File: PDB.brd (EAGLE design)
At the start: 125.9 x 103 mm, 76 parts

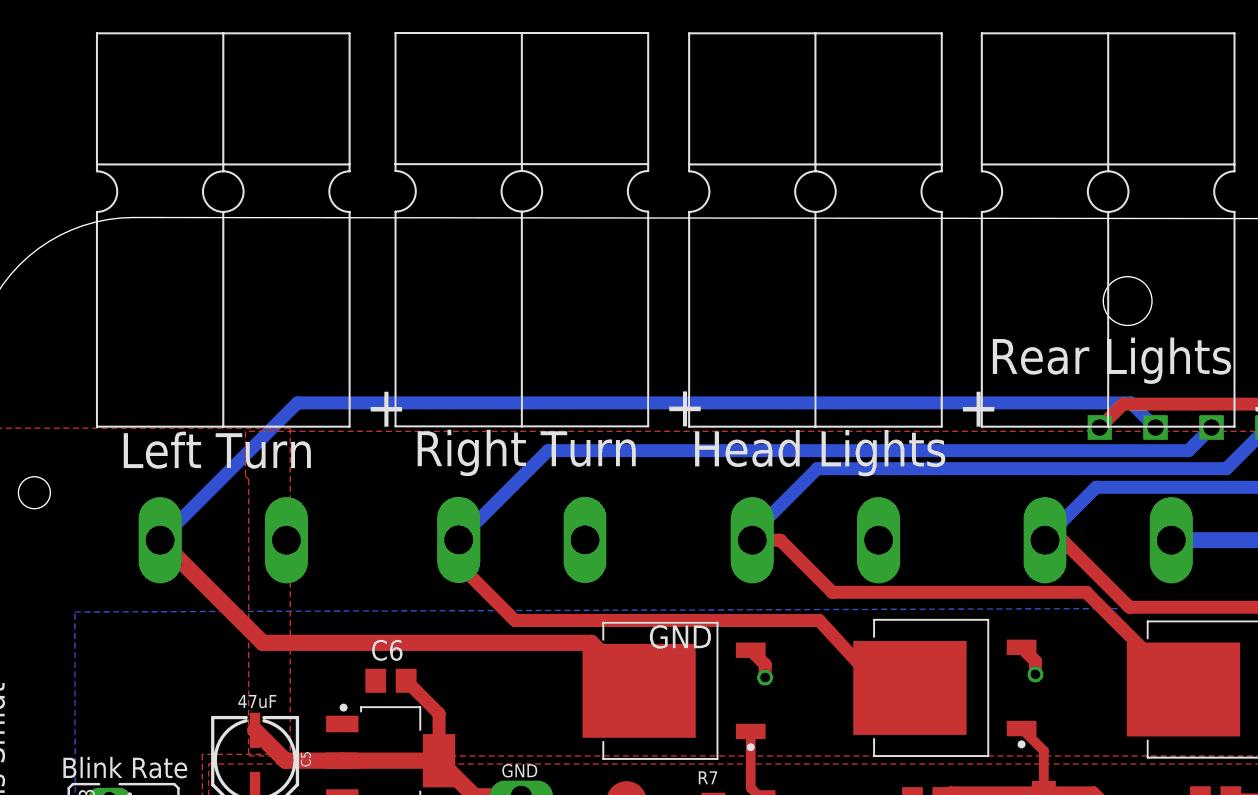
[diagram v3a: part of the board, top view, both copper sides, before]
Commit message: Deleted Anderson connector for left and right light
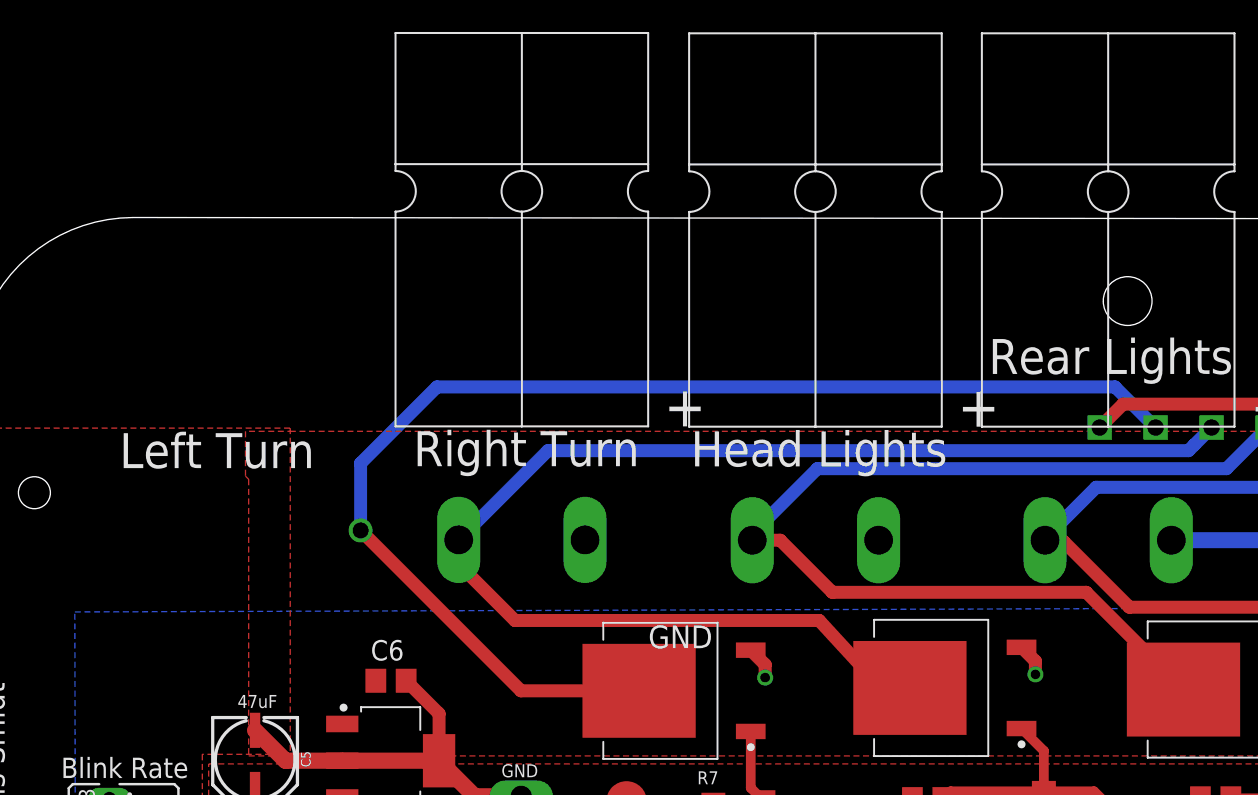
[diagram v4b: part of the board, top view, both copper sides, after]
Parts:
- removed HAZL_OUT: POWERPOLE_POWER25A_HORIZONTAL_G2, powerpoles:POWERPOLE_PAIR_25A_HORIZ_G2
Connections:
- net HAZ_L_SIG: no longer HAZL_OUT.BLACK
- net VDD: no longer HAZL_OUT.RED
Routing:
- net HAZ_L_SIG: track 100.3 -> 78.5 mm, vias 0 -> 1
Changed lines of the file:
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@@
 <drawing>
 <settings>
-<setting alwaysvectorfont="no"/>
+<setting alwaysvectorfont="yes"/>
 <setting verticaltext="up"/>
 </settings>
@@
 <text x="91.5" y="134.82" size="0.6096" layer="26">GND</text>
 <text x="80.06" y="131.94" size="0.6096" layer="26">TURN_R</text>
-<text x="76.94" y="134.76" size="0.6096" layer="26">TURN_L</text>
+<text x="77.04" y="134.56" size="0.6096" layer="26">TURN_L</text>
 <text x="73.52" y="134.76" size="0.6096" layer="26">BRAKE</text>
 <text x="84.9" y="131.94" size="0.6096" layer="26">HL</text>
@@
 <element name="ADD1_OUT" library="powerpoles" package="POWERPOLE_PAIR_25A_HORIZ_G2" value="POWERPOLE_POWER25A_HORIZONTAL_G2" x="55.604" y="52.08" smashed="yes" rot="R180"/>
 <element name="WIPER_OUT" library="powerpoles" package="POWERPOLE_PAIR_25A_HORIZ_G2" value="POWERPOLE_POWER25A_HORIZONTAL_G2" x="35.64" y="51.84" smashed="yes" rot="R180"/>
-<element name="HAZL_OUT" library="powerpoles" package="POWERPOLE_PAIR_25A_HORIZ_G2" value="POWERPOLE_POWER25A_HORIZONTAL_G2" x="20.012" y="133.69" smashed="yes"/>
 <element name="HAZR_OUT" library="powerpoles" package="POWERPOLE_PAIR_25A_HORIZ_G2" value="POWERPOLE_POWER25A_HORIZONTAL_G2" x="38.684" y="133.71" smashed="yes"/>
 <element name="BRAKE_OUT" library="powerpoles" package="POWERPOLE_PAIR_25A_HORIZ_G2" value="POWERPOLE_POWER25A_HORIZONTAL_G2" x="96.232" y="133.49" smashed="yes"/>
@@
 <signals>
 <signal name="VDD">
-<contactref element="HAZL_OUT" pad="RED"/>
 <contactref element="HAZR_OUT" pad="RED"/>
 <contactref element="HEADLIGHTS_OUT" pad="RED"/>
@@
 </signal>
 <signal name="HAZ_L_SIG">
-<contactref element="HAZ_L" pad="3"/>
-<contactref element="HAZL_OUT" pad="BLACK"/>
 <contactref element="LIGHTS" pad="P2"/>
-<wire x1="76.776" y1="135.176" x2="24.648" y2="135.176" width="0.8128" layer="16"/>
-<wire x1="24.648" y1="135.176" x2="16.062" y2="126.59" width="0.8128" layer="16"/>
-<wire x1="78.316" y1="133.636" x2="76.776" y2="135.176" width="0.8128" layer="16"/>
-<wire x1="43.01668125" y1="120.172" x2="22.48" y2="120.172" width="1.016" layer="1"/>
-<wire x1="22.48" y1="120.172" x2="16.062" y2="126.59" width="1.016" layer="1"/>
-<wire x1="46.01668125" y1="117.172" x2="43.01668125" y2="120.172" width="1.016" layer="1"/>
+<wire x1="75.776" y1="136.176" x2="78.316" y2="133.636" width="0.8128" layer="16"/>
+<contactref element="HAZ_L" pad="3"/>
+<wire x1="46.01668125" y1="117.172" x2="38.628" y2="117.172" width="0.8128" layer="1"/>
+<via x="28.6" y="127.2" extent="1-16" drill="1"/>
+<wire x1="38.628" y1="117.172" x2="28.6" y2="127.2" width="0.8128" layer="1"/>
+<wire x1="28.6" y1="127.2" x2="28.6" y2="131.4" width="0.8128" layer="16"/>
+<wire x1="33.376" y1="136.176" x2="75.776" y2="136.176" width="0.8128" layer="16"/>
+<wire x1="28.6" y1="131.4" x2="33.376" y2="136.176" width="0.8128" layer="16"/>
 </signal>
 <signal name="BRAKE_SIG">

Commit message: Last time forget to save. This is the real version of last commit.
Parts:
- removed ADD1_OUT, HAZR_OUT: POWERPOLE_POWER25A_HORIZONTAL_G2, powerpoles:POWERPOLE_PAIR_25A_HORIZ_G2
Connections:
- removed net N$17: ADD1.3, ADD1_OUT.BLACK
- net HAZ_R_SIG: no longer HAZR_OUT.BLACK
- net VDD: no longer ADD1_OUT.RED, HAZR_OUT.RED
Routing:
- net HAZ_L_SIG: track 78.5 -> 50.2 mm
- net HAZ_R_SIG: track 83.0 -> 58.4 mm, vias 0 -> 1
- net N$17: track 8.79 -> 0.00 mm
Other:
- board text removed: "Left Turn"
- board text removed: "Right Turn"
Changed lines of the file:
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@@
 <text x="7.287" y="86.841" size="2.54" layer="25" font="vector" ratio="13" rot="R90">SEM 2019</text>
 <text x="8.21" y="56.622" size="3.81" layer="25" rot="R90">REVolution</text>
-<text x="31.904" y="131.22" size="2.1844" layer="25">Right Turn </text>
-<text x="13.52" y="131.1" size="2.1844" layer="25">Left Turn </text>
 <text x="64.746" y="64.275" size="1.27" layer="25">GND</text>
 <text x="46.588" y="119.834" size="1.4224" layer="25">GND</text>
@@
 <elements>
 <element name="ADD1" library="master_library" package="TO254P1054X240-3" package3d_urn="urn:adsk.eagle:package:8893803/1" value="NCV8405ADPAK-3PIN" x="56.654" y="68.958" smashed="yes" rot="R270"/>
-<element name="ADD1_OUT" library="powerpoles" package="POWERPOLE_PAIR_25A_HORIZ_G2" value="POWERPOLE_POWER25A_HORIZONTAL_G2" x="55.604" y="52.08" smashed="yes" rot="R180"/>
 <element name="WIPER_OUT" library="powerpoles" package="POWERPOLE_PAIR_25A_HORIZ_G2" value="POWERPOLE_POWER25A_HORIZONTAL_G2" x="35.64" y="51.84" smashed="yes" rot="R180"/>
-<element name="HAZR_OUT" library="powerpoles" package="POWERPOLE_PAIR_25A_HORIZ_G2" value="POWERPOLE_POWER25A_HORIZONTAL_G2" x="38.684" y="133.71" smashed="yes"/>
 <element name="BRAKE_OUT" library="powerpoles" package="POWERPOLE_PAIR_25A_HORIZ_G2" value="POWERPOLE_POWER25A_HORIZONTAL_G2" x="96.232" y="133.49" smashed="yes"/>
 <element name="HEADLIGHTS_OUT" library="powerpoles" package="POWERPOLE_PAIR_25A_HORIZ_G2" value="POWERPOLE_POWER25A_HORIZONTAL_G2" x="57.044" y="133.69" smashed="yes"/>
@@
 <signals>
 <signal name="VDD">
-<contactref element="HAZR_OUT" pad="RED"/>
 <contactref element="HEADLIGHTS_OUT" pad="RED"/>
 <contactref element="C10" pad="+"/>
 <contactref element="D1" pad="C"/>
-<contactref element="ADD1_OUT" pad="RED"/>
 <contactref element="LM2940" pad="1"/>
 <contactref element="TRACO" pad="1"/>
@@
 <wire x1="106" y1="126.952" x2="99.316" y2="133.636" width="1.27" layer="16"/>
 </signal>
-<signal name="N$17">
-<contactref element="ADD1" pad="3"/>
-<contactref element="ADD1_OUT" pad="BLACK"/>
-<wire x1="59.554" y1="59.18" x2="56.654" y2="62.08" width="1.27" layer="1"/>
-<wire x1="56.654" y1="62.08" x2="56.654" y2="66.773" width="1.27" layer="1"/>
-</signal>
 <signal name="N$19">
 <contactref element="WIPER_" pad="3"/>
@@
 <signal name="HAZ_L_SIG">
 <contactref element="LIGHTS" pad="P2"/>
-<wire x1="75.776" y1="136.176" x2="78.316" y2="133.636" width="0.8128" layer="16"/>
 <contactref element="HAZ_L" pad="3"/>
-<wire x1="46.01668125" y1="117.172" x2="38.628" y2="117.172" width="0.8128" layer="1"/>
-<via x="28.6" y="127.2" extent="1-16" drill="1"/>
-<wire x1="38.628" y1="117.172" x2="28.6" y2="127.2" width="0.8128" layer="1"/>
-<wire x1="28.6" y1="127.2" x2="28.6" y2="131.4" width="0.8128" layer="16"/>
-<wire x1="33.376" y1="136.176" x2="75.776" y2="136.176" width="0.8128" layer="16"/>
-<wire x1="28.6" y1="131.4" x2="33.376" y2="136.176" width="0.8128" layer="16"/>
+<via x="46.1" y="127.2" extent="1-16" drill="0.8128"/>
+<wire x1="46.1" y1="127.2" x2="46.1" y2="117.25531875" width="0.8128" layer="1"/>
+<wire x1="46.01668125" y1="117.172" x2="46.1" y2="117.25531875" width="0.8128" layer="1"/>
+<wire x1="46.1" y1="127.2" x2="46.1" y2="132.5" width="0.8128" layer="16"/>
+<wire x1="46.1" y1="132.5" x2="49.8" y2="136.2" width="0.8128" layer="16"/>
+<wire x1="49.8" y1="136.2" x2="75.752" y2="136.2" width="0.8128" layer="16"/>
+<wire x1="75.752" y1="136.2" x2="78.316" y2="133.636" width="0.8128" layer="16"/>
 </signal>
 <signal name="BRAKE_SIG">
@@
 <contactref element="LIGHTS" pad="P3"/>
 <contactref element="HAZ_R" pad="3"/>
-<contactref element="HAZR_OUT" pad="BLACK"/>
-<wire x1="38.254" y1="121.57" x2="57.278834375" y2="121.57" width="0.8128" layer="1"/>
-<wire x1="81.816" y1="133.636" x2="80.74" y2="132.56" width="0.8128" layer="16"/>
-<wire x1="80.74" y1="132.56" x2="80.37" y2="132.19" width="0.8128" layer="16"/>
-<wire x1="80.37" y1="132.19" x2="40.314" y2="132.19" width="0.8128" layer="16"/>
-<wire x1="40.314" y1="132.19" x2="34.734" y2="126.61" width="0.8128" layer="16"/>
-<wire x1="61.159009375" y1="117.352" x2="57.278834375" y2="121.57" width="0.8128" layer="1"/>
-<wire x1="62.951" y1="117.352" x2="61.159009375" y2="117.352" width="1.27" layer="1"/>
-<wire x1="34.734" y1="126.61" x2="34.734" y2="125.09" width="0.8128" layer="1"/>
-<wire x1="34.734" y1="125.09" x2="38.254" y2="121.57" width="0.8128" layer="1"/>
+<wire x1="62.951" y1="117.352" x2="59.648" y2="117.352" width="0.8128" layer="1"/>
+<wire x1="62.951" y1="117.352" x2="57.948" y2="117.352" width="0.8128" layer="1"/>
+<wire x1="57.948" y1="117.352" x2="48.2" y2="127.1" width="0.8128" layer="1"/>
+<wire x1="48.2" y1="127.1" x2="48.25" y2="127.15" width="0.8128" layer="1"/>
+<via x="48.25" y="127.15" extent="1-16" drill="0.8128"/>
+<wire x1="48.25" y1="127.15" x2="53.2" y2="132.1" width="0.8128" layer="16"/>
+<wire x1="53.2" y1="132.1" x2="80.28" y2="132.1" width="0.8128" layer="16"/>
+<wire x1="80.28" y1="132.1" x2="81.816" y2="133.636" width="0.8128" layer="16"/>
 </signal>
 <signal name="EXT_CLK">
